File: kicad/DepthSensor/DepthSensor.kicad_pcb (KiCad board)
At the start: 2 copper layers, 80.5 x 106 mm, 40 parts, among them J1 PJ-102AH, J2 J_SNS, J3 J_PANEL, J4 J_SPARE, U1 ESP32-C6-DevKitM-1, U2 TBD62783APG

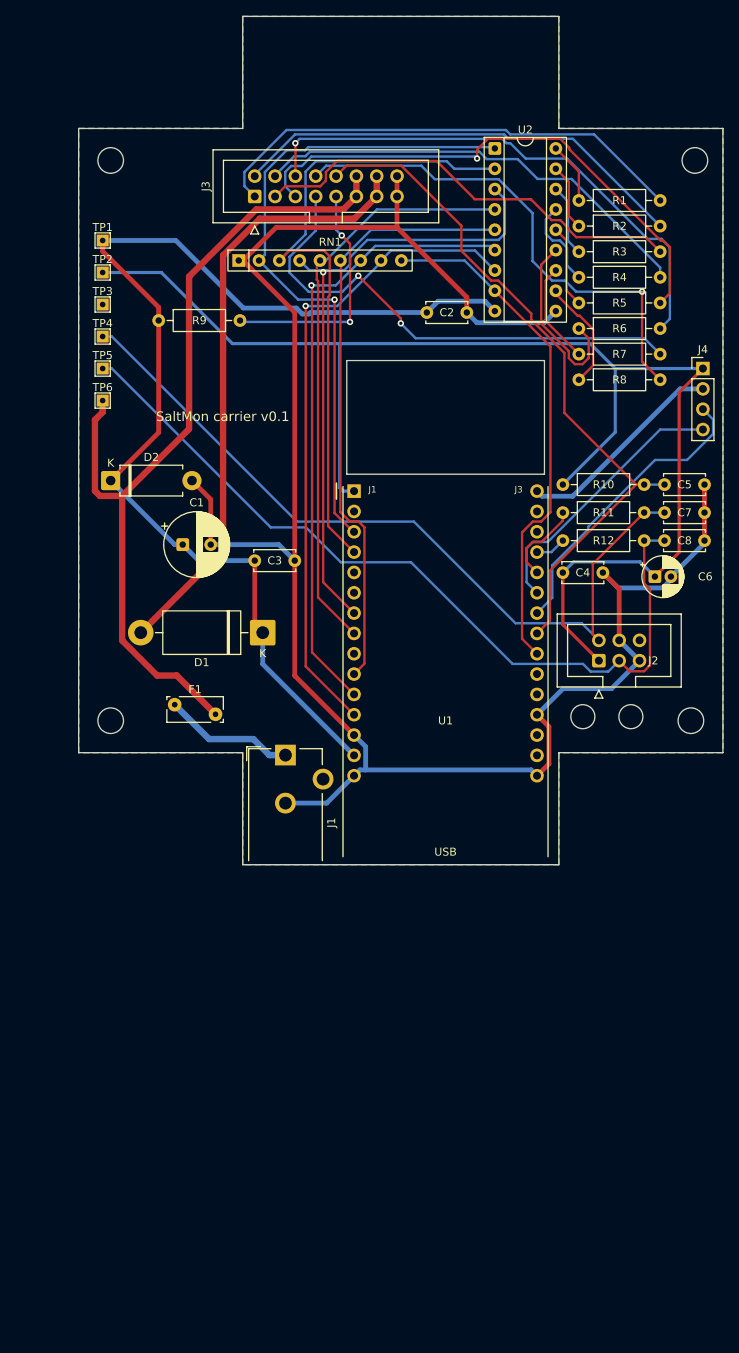
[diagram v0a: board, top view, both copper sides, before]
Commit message: Add lid panel PCB rev 0.1, lid pick list; carrier rev 0.2 without top tab
- kicad/LidPanel: passive lid board (8 flat-top 5 mm LEDs, J1 right-angle 2x8,
  pads for the panel switch and button), routed, with a 1:1 lid drilling
  template on User.Drawings
- kicad/lib: shared schgen/pcbgen helpers used by both boards
- Carrier rev 0.2: top tab removed (80.5 x 92 mm), rerouted
- docs: lid-pick-list.md with DigiKey part numbers; pick list, requirements
  v0.8, pin map, README and CHANGELOG updated for the lid board
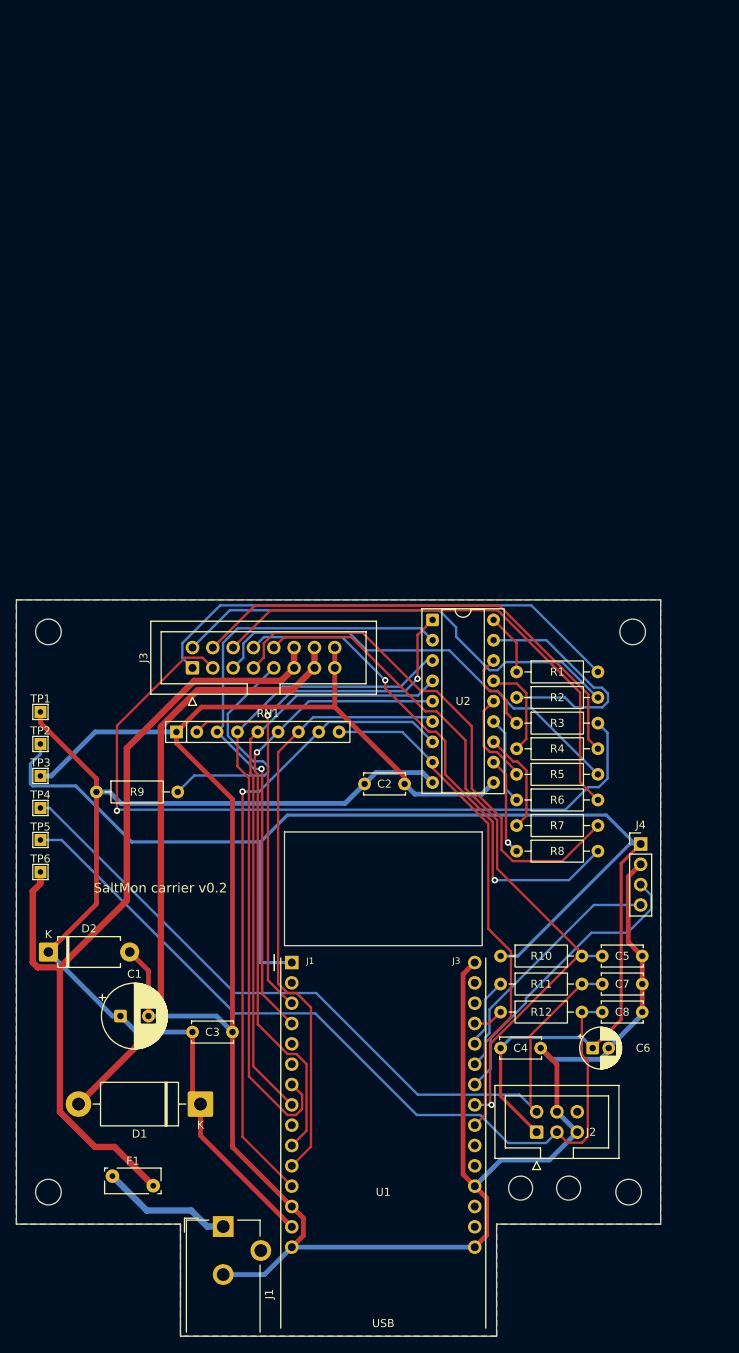
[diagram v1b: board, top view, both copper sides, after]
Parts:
- moved C4 59.9 mm to (160.5, 170.0)
- moved J4 59.9 mm to (178.0, 144.5)
- moved R5 59.4 mm to (162.5, 135.8)
- moved C1 59.4 mm to (113.0, 166.0)
- moved C2 59.4 mm to (143.5, 137.0)
- moved C3 59.4 mm to (122.0, 168.0)
- moved C5 59.4 mm to (173.2, 158.5)
- moved C6 59.4 mm to (172.0, 170.0)
- moved C7 59.4 mm to (173.2, 162.0)
- moved C8 59.4 mm to (173.2, 165.5)
- moved D1 59.4 mm to (123.0, 177.0)
- moved D2 59.4 mm to (104.0, 158.0)
- moved F1 59.4 mm to (112.0, 186.0)
- moved H1 59.4 mm to (104.0, 118.0)
- moved H2 59.4 mm to (177.0, 118.0)
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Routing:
- net /LED_A3: track 55.4 -> 97.0 mm, vias 0 -> 1
- net /GND: track 265.4 -> 299.9 mm
- net /DRV_O2: track 8.35 -> 30.3 mm
- net /DRV_O6: track 23.0 -> 11.0 mm
- net /LED_A5: track 67.4 -> 55.8 mm, vias 1 -> 0
- net /+3V3: track 171.3 -> 182.2 mm
- net /V_SYS: track 141.0 -> 131.7 mm
- net /LED_CH1: track 83.0 -> 75.4 mm, vias 1 -> 2
- net /LED_CH3: track 79.1 -> 84.3 mm, vias 1 -> 0
- net /LED_A4: track 56.7 -> 61.0 mm
- net /LED_A6: track 67.4 -> 63.9 mm, vias 1 -> 0
- net /LED_A7: track 63.4 -> 66.4 mm, vias 2 -> 0
- net /LED_CH5: track 75.1 -> 77.9 mm, vias 0 -> 1
- net /LED_CH2: track 82.5 -> 79.8 mm, vias 0 -> 1
- net /BTN_N: track 88.5 -> 91.0 mm, vias 0 -> 1
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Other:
- board size 80.5 x 106 mm -> 80.5 x 92 mm
- board text added: "SaltMon carrier v0.2"
- board text removed: "SaltMon carrier v0.1"
